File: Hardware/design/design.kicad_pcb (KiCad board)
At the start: 2 copper layers, 1 part

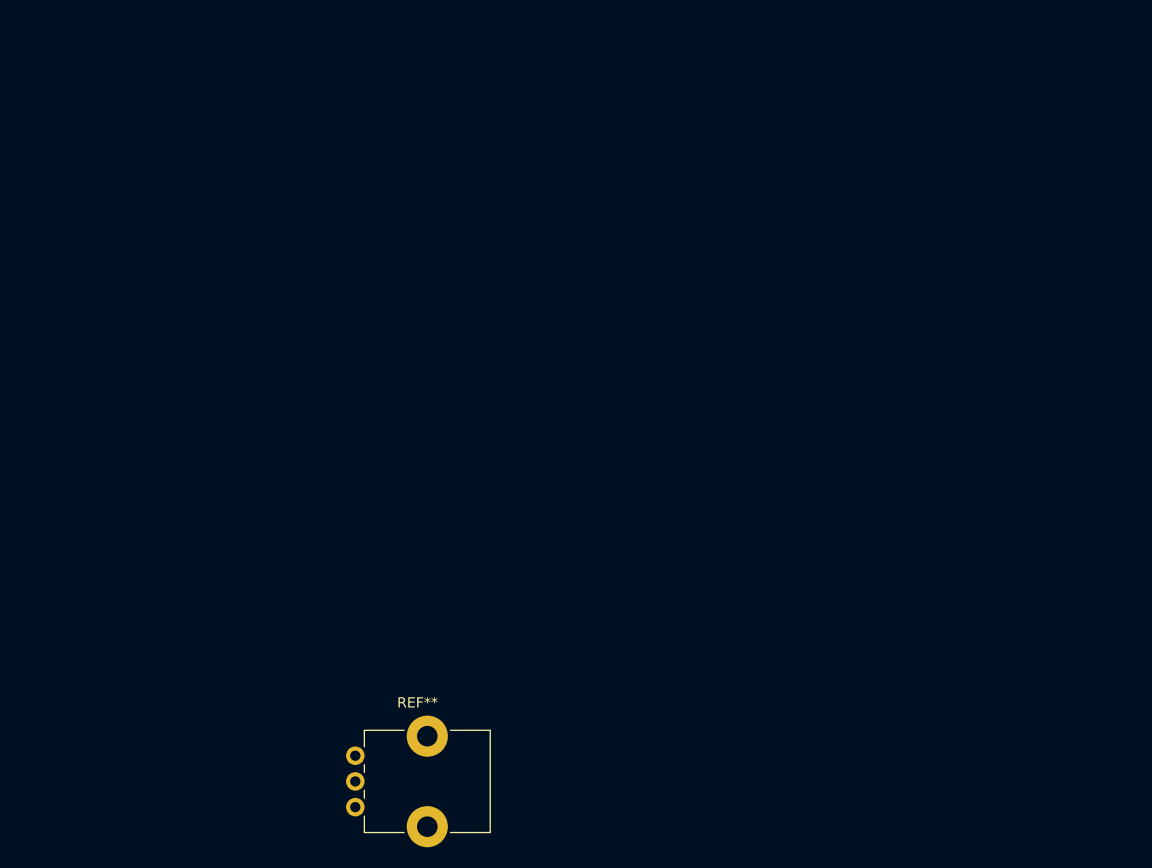
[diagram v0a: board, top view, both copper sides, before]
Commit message: chose and added 3 toggle switches
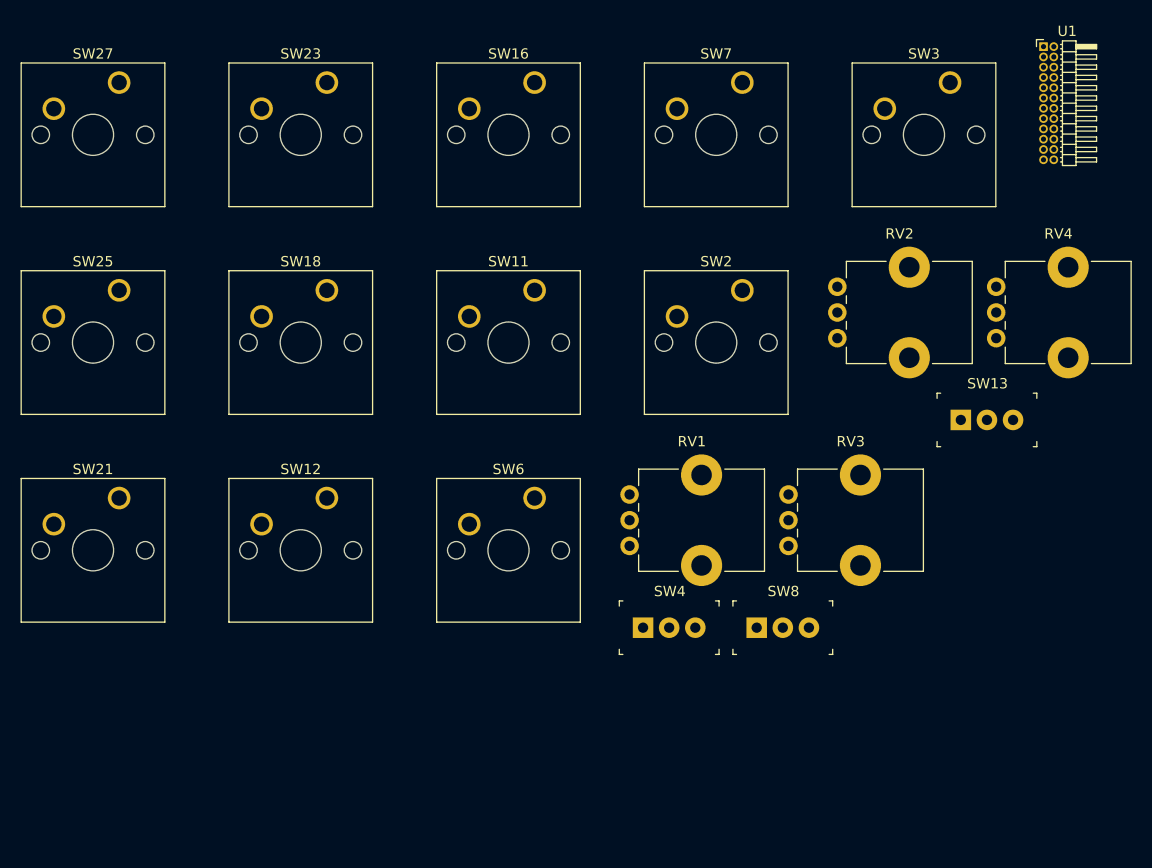
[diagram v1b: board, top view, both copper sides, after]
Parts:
- removed REF**: Potentiometer_Bourns_PTV09A-1_Single_Vertical, Potentiometer_THT:Potentiometer_Bourns_PTV09A-1_Single_Vertical
- added RV1: R_POT, Potentiometer_THT:Potentiometer_Bourns_PTV09A-1_Single_Vertical, F.Cu at (121.9, 52.1)
- added RV2: R_POT, Potentiometer_THT:Potentiometer_Bourns_PTV09A-1_Single_Vertical, F.Cu at (142.1, 31.9)
- added RV3: R_POT, Potentiometer_THT:Potentiometer_Bourns_PTV09A-1_Single_Vertical, F.Cu at (137.4, 52.1)
- added RV4: R_POT, Potentiometer_THT:Potentiometer_Bourns_PTV09A-1_Single_Vertical, F.Cu at (157.6, 31.9)
- added SW11: SW_Push, Button_Switch_Keyboard:SW_Cherry_MX_1.00u_PCB, F.Cu at (112.7, 27.2)
- added SW12: SW_Push, Button_Switch_Keyboard:SW_Cherry_MX_1.00u_PCB, F.Cu at (92.5, 47.4)
- added SW13: SW_Push, digikey-footprints:Switch_Toggle_ATE1D-2M3-10-Z, F.Cu at (156.7, 39.8)
- added SW16: SW_Push, Button_Switch_Keyboard:SW_Cherry_MX_1.00u_PCB, F.Cu at (112.7, 7.01)
- added SW18: SW_Push, Button_Switch_Keyboard:SW_Cherry_MX_1.00u_PCB, F.Cu at (92.5, 27.2)
- added SW2: SW_Push, Button_Switch_Keyboard:SW_Cherry_MX_1.00u_PCB, F.Cu at (132.9, 27.2)
- added SW21: SW_Push, Button_Switch_Keyboard:SW_Cherry_MX_1.00u_PCB, F.Cu at (72.3, 47.4)
- added SW23: SW_Push, Button_Switch_Keyboard:SW_Cherry_MX_1.00u_PCB, F.Cu at (92.5, 7.01)
- added SW25: SW_Push, Button_Switch_Keyboard:SW_Cherry_MX_1.00u_PCB, F.Cu at (72.3, 27.2)
- added SW27: SW_Push, Button_Switch_Keyboard:SW_Cherry_MX_1.00u_PCB, F.Cu at (72.3, 7.01)
- added SW3: SW_Push, Button_Switch_Keyboard:SW_Cherry_MX_1.00u_PCB, F.Cu at (153.1, 7.01)
- added SW4: SW_Push, digikey-footprints:Switch_Toggle_ATE1D-2M3-10-Z, F.Cu at (125.8, 60.0)
- added SW6: SW_Push, Button_Switch_Keyboard:SW_Cherry_MX_1.00u_PCB, F.Cu at (112.7, 47.4)
- added SW7: SW_Push, Button_Switch_Keyboard:SW_Cherry_MX_1.00u_PCB, F.Cu at (132.9, 7.01)
- added SW8: SW_Push, digikey-footprints:Switch_Toggle_ATE1D-2M3-10-Z, F.Cu at (136.8, 60.0)
- added U1: ProMicro, Connector_PinHeader_1.00mm:PinHeader_2x12_P1.00mm_Horizontal, F.Cu at (162.2, 3.52)

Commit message: chose rotary switches and diodes, organized layout a bit
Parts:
- added D1: DIODE, Diode_THT:D_5KPW_P7.62mm_Vertical_AnodeUp, F.Cu at (397.5, 88.9)
- added D10: DIODE, Diode_THT:D_5KPW_P7.62mm_Vertical_AnodeUp, F.Cu at (378.5, 74.9)
- added D11: DIODE, Diode_THT:D_5KPW_P7.62mm_Vertical_AnodeUp, F.Cu at (396.2, 58.4)
- added D12: DIODE, Diode_THT:D_5KPW_P7.62mm_Vertical_AnodeUp, F.Cu at (359.4, 74.9)
- added D13: DIODE, Diode_THT:D_5KPW_P7.62mm_Vertical_AnodeUp, F.Cu at (38.1, 157.5)
- added D14: DIODE, Diode_THT:D_5KPW_P7.62mm_Vertical_AnodeUp, F.Cu at (35.6, 193.0)
- added D15: DIODE, Diode_THT:D_5KPW_P7.62mm_Vertical_AnodeUp, F.Cu at (33.0, 229.9)
- added D16: DIODE, Diode_THT:D_5KPW_P7.62mm_Vertical_AnodeUp, F.Cu at (29.2, 265.4)
- added D17: DIODE, Diode_THT:D_5KPW_P7.62mm_Vertical_AnodeUp, F.Cu at (58.4, 157.5)
- added D18: DIODE, Diode_THT:D_5KPW_P7.62mm_Vertical_AnodeUp, F.Cu at (57.1, 194.3)
- added D19: DIODE, Diode_THT:D_5KPW_P7.62mm_Vertical_AnodeUp, F.Cu at (55.9, 229.9)
- added D2: DIODE, Diode_THT:D_5KPW_P7.62mm_Vertical_AnodeUp, F.Cu at (378.5, 105.4)
- added D20: DIODE, Diode_THT:D_5KPW_P7.62mm_Vertical_AnodeUp, F.Cu at (53.3, 265.4)
- added D21: DIODE, Diode_THT:D_5KPW_P7.62mm_Vertical_AnodeUp, F.Cu at (81.3, 157.5)
- added D22: DIODE, Diode_THT:D_5KPW_P7.62mm_Vertical_AnodeUp, F.Cu at (78.7, 194.3)
- added D23: DIODE, Diode_THT:D_5KPW_P7.62mm_Vertical_AnodeUp, F.Cu at (77.5, 227.3)
- added D24: DIODE, Diode_THT:D_5KPW_P7.62mm_Vertical_AnodeUp, F.Cu at (74.9, 265.4)
- added D25: DIODE, Diode_THT:D_5KPW_P7.62mm_Vertical_AnodeUp, F.Cu at (101.6, 160.0)
- added D26: DIODE, Diode_THT:D_5KPW_P7.62mm_Vertical_AnodeUp, F.Cu at (99.1, 194.3)
- added D27: DIODE, Diode_THT:D_5KPW_P7.62mm_Vertical_AnodeUp, F.Cu at (99.1, 228.6)
- added D28: DIODE, Diode_THT:D_5KPW_P7.62mm_Vertical_AnodeUp, F.Cu at (97.8, 264.2)
- added D29: DIODE, Diode_THT:D_5KPW_P7.62mm_Vertical_AnodeUp, F.Cu at (120.7, 160.0)
- added D3: DIODE, Diode_THT:D_5KPW_P7.62mm_Vertical_AnodeUp, F.Cu at (377.2, 88.9)
- added D30: DIODE, Diode_THT:D_5KPW_P7.62mm_Vertical_AnodeUp, F.Cu at (120.7, 194.3)
- added D31: DIODE, Diode_THT:D_5KPW_P7.62mm_Vertical_AnodeUp, F.Cu at (120.7, 228.6)
- added D32: DIODE, Diode_THT:D_5KPW_P7.62mm_Vertical_AnodeUp, F.Cu at (119.4, 264.2)
- added D33: DIODE, Diode_THT:D_5KPW_P7.62mm_Vertical_AnodeUp, F.Cu at (144.8, 160.0)
- added D34: DIODE, Diode_THT:D_5KPW_P7.62mm_Vertical_AnodeUp, F.Cu at (142.2, 194.3)
- added D35: DIODE, Diode_THT:D_5KPW_P7.62mm_Vertical_AnodeUp, F.Cu at (142.2, 228.6)
- added D36: DIODE, Diode_THT:D_5KPW_P7.62mm_Vertical_AnodeUp, F.Cu at (141.0, 265.4)
- added D4: DIODE, Diode_THT:D_5KPW_P7.62mm_Vertical_AnodeUp, F.Cu at (358.1, 105.4)
- added D5: DIODE, Diode_THT:D_5KPW_P7.62mm_Vertical_AnodeUp, F.Cu at (358.1, 88.9)
- added D6: DIODE, Diode_THT:D_5KPW_P7.62mm_Vertical_AnodeUp, F.Cu at (397.5, 105.4)
- added D7: DIODE, Diode_THT:D_5KPW_P7.62mm_Vertical_AnodeUp, F.Cu at (359.4, 58.4)
- added D8: DIODE, Diode_THT:D_5KPW_P7.62mm_Vertical_AnodeUp, F.Cu at (397.5, 74.9)
- added D9: DIODE, Diode_THT:D_5KPW_P7.62mm_Vertical_AnodeUp, F.Cu at (377.2, 58.4)
- added SW1: NKK_NR01, Kicad_Akiyuki_Footprint:NR01, F.Cu at (341.6, 90.2)
- added SW10: NKK_NR01, Kicad_Akiyuki_Footprint:NR01, F.Cu at (341.6, 105.4)
- added SW14: SW_Push, Button_Switch_Keyboard:SW_Cherry_MX_1.00u_PCB, F.Cu at (76.2, 280.7)
- added SW15: NKK_NR01, Kicad_Akiyuki_Footprint:NR01, F.Cu at (341.6, 59.7)
- added SW17: SW_Push, Button_Switch_Keyboard:SW_Cherry_MX_1.00u_PCB, F.Cu at (102.9, 242.6)
- added SW19: SW_Push, Button_Switch_Keyboard:SW_Cherry_MX_1.00u_PCB, F.Cu at (100.3, 278.1)
- added SW20: NKK_NR01, Kicad_Akiyuki_Footprint:NR01, F.Cu at (341.6, 74.9)
- added SW22: SW_Push, Button_Switch_Keyboard:SW_Cherry_MX_1.00u_PCB, F.Cu at (125.7, 242.6)
- added SW24: SW_Push, Button_Switch_Keyboard:SW_Cherry_MX_1.00u_PCB, F.Cu at (123.2, 278.1)
- added SW26: SW_Push, Button_Switch_Keyboard:SW_Cherry_MX_1.00u_PCB, F.Cu at (144.8, 242.6)
- added SW28: SW_Push, Button_Switch_Keyboard:SW_Cherry_MX_1.00u_PCB, F.Cu at (146.1, 278.1)
- added SW5: SW_Push, digikey-footprints:Tilt_Switch_RB-220-07A_R, F.Cu at (29.2, 283.2)
- added SW9: SW_Push, digikey-footprints:Tilt_Switch_RB-220-07A_R, F.Cu at (53.3, 281.9)
- U1: footprint Connector_PinHeader_1.00mm:PinHeader_2x12_P1.00mm_Horizontal -> promicro:ProMicro
- moved SW3 227.2 mm to (40.6, 204.5)
- moved SW13 218.4 mm to (78.7, 243.8)
- moved SW27 212.4 mm to (147.3, 205.7)
- moved SW7 209.7 mm to (62.2, 204.5)
- moved SW4 204.8 mm to (35.6, 243.8)
- moved SW23 201.5 mm to (125.7, 205.7)
- moved SW8 199.8 mm to (58.4, 243.8)
- moved SW18 178.9 mm to (104.1, 205.7)
- moved SW2 171.6 mm to (41.9, 172.7)
- moved SW16 165.8 mm to (106.7, 172.7)
- moved SW25 164.3 mm to (148.6, 172.7)
- moved RV4 162.9 mm to (232.4, 176.5)
- moved SW12 157.4 mm to (82.5, 204.5)
- moved RV2 154.7 mm to (232.4, 157.5)
- moved SW11 148.3 mm to (83.8, 172.7)
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
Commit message: semi-linearized switch matrix into 2 octave layout
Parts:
- SW13, SW4, SW8: footprint digikey-footprints:Switch_Toggle_ATE1D-2M3-10-Z -> Button_Switch_Keyboard:SW_Cherry_MX_1.00u_PCB
- SW5, SW9: footprint digikey-footprints:Tilt_Switch_RB-220-07A_R -> Button_Switch_Keyboard:SW_Cherry_MX_1.00u_PCB
- moved SW25 231.8 mm to (-83.0, 180.5)
- moved SW21 229.2 mm to (-102.1, 180.5)
- moved D33 228.7 mm to (-83.0, 180.5)
- moved D29 223.7 mm to (-102.1, 180.5)
- moved SW16 218.6 mm to (-111.6, 161.5)
- moved D25 213.2 mm to (-111.6, 161.5)
- moved SW11 205.1 mm to (-121.1, 180.5)
- moved D21 203.7 mm to (-121.1, 180.5)
- moved SW6 193.2 mm to (-130.7, 161.5)
- moved D17 189.1 mm to (-130.7, 161.5)
- moved SW2 182.3 mm to (-140.2, 180.5)
- moved D13 179.8 mm to (-140.2, 180.5)
- moved SW27 175.0 mm to (-25.9, 180.5)
- moved D34 168.7 mm to (-25.9, 180.5)
- moved SW23 167.1 mm to (-35.4, 161.5)
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
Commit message: columns routed together
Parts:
- moved D32 5.68 mm to (95.4, 166.6)
- moved D28 1.56 mm to (88.4, 180.5)
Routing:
- net /ROW1: track 0.00 -> 115.0 mm
- net /ROW3: track 0.00 -> 115.0 mm
- net /ROW2: track 0.00 -> 112.6 mm
- net /ROW0: track 0.00 -> 111.2 mm

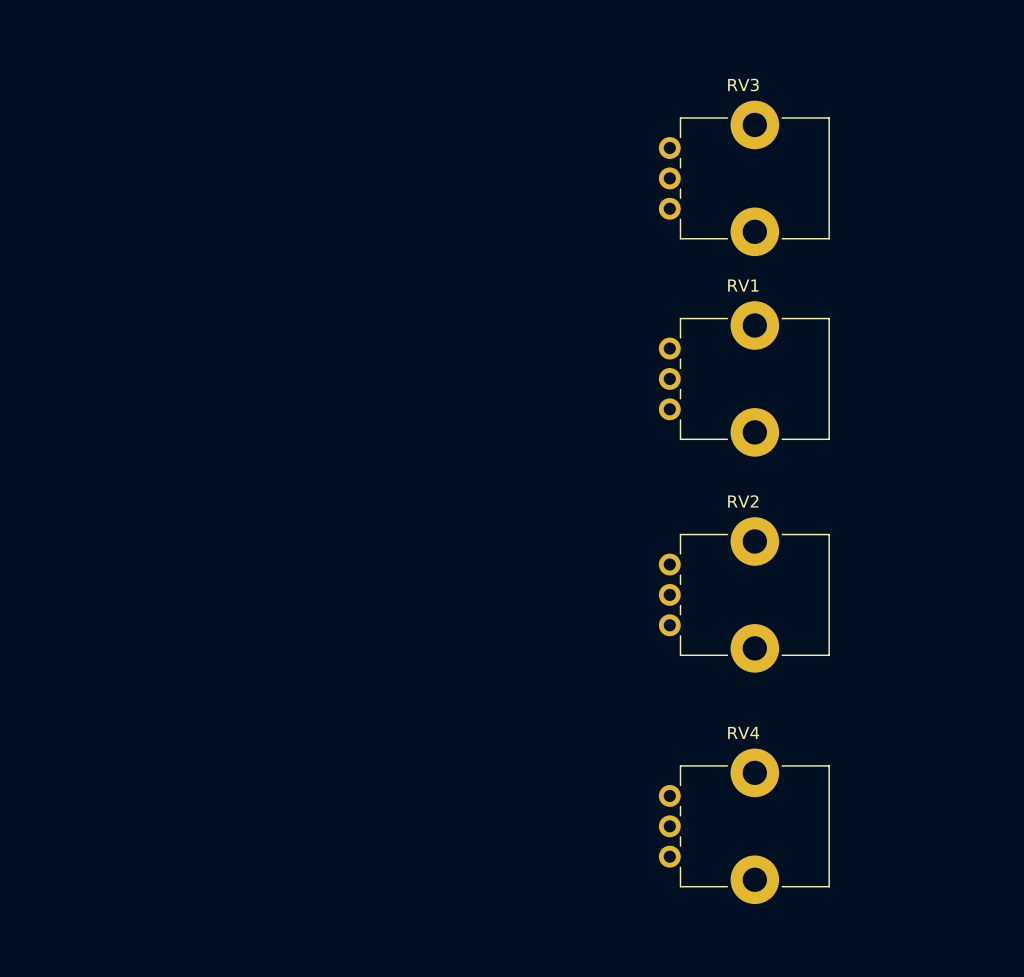
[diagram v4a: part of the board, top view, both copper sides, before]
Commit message: routed vcc and gnd for pots
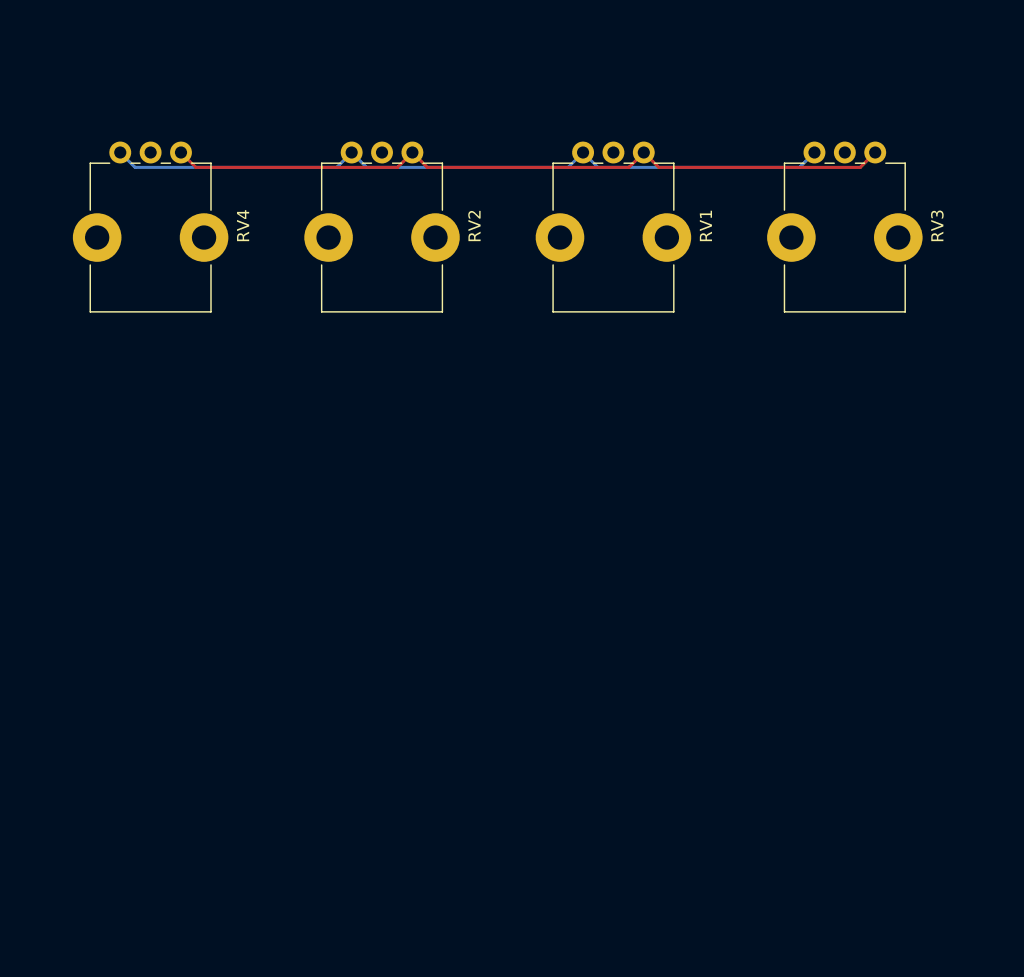
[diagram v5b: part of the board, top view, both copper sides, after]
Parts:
- moved RV4 73.5 mm to (187.2, 118.6), turned to 270 degrees
- moved RV2 46.9 mm to (206.2, 118.6), turned to 270 degrees
- moved RV1 22.3 mm to (225.3, 118.6), turned to 270 degrees
- moved RV3 12.8 mm to (244.3, 118.6), turned to 270 degrees
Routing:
- net /VCC: track 0.00 -> 60.2 mm
- net /GND: track 0.00 -> 60.2 mm

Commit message: a less elegant solution to column routing
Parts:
- moved D32 5.68 mm to (97.9, 161.5)
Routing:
- net /COL3: track 0.00 -> 265.3 mm, vias 0 -> 7
- net /COL1: track 0.00 -> 247.3 mm, vias 0 -> 7
- net /COL0: track 0.00 -> 245.6 mm, vias 0 -> 3
- net /COL4: track 0.00 -> 237.8 mm, vias 0 -> 3
- net /COL2: track 0.00 -> 237.6 mm, vias 0 -> 7
- net /COL5: track 0.00 -> 229.8 mm, vias 0 -> 3
- net /GND: track 60.2 -> 79.0 mm
- net /ROW2: track 112.6 -> 111.0 mm

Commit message: finished column routing, sitched to 1206 SMD diodes
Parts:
- D1, D10, D11, D12, D13, D14, D15, D16, D17, D18, D19, D2, D20, D21, D22, D23, D24, D25, D26, D27, D28, D29, D3, D30, D31, D32, D33, D34, D35, D36, D4, D5, D6, D7, D8, D9: footprint Diode_THT:D_5KPW_P7.62mm_Vertical_AnodeUp -> Diode_SMD:D_1206_3216Metric
- moved D13 202.0 mm to (21.4, 59.3), turned to 270 degrees
- moved D14 202.0 mm to (88.0, 40.2), turned to 270 degrees
- moved D15 202.0 mm to (154.7, 59.3), turned to 270 degrees
- moved D16 202.0 mm to (221.4, 40.2), turned to 270 degrees
- moved D17 202.0 mm to (30.9, 40.2), turned to 270 degrees
- moved D18 202.0 mm to (97.6, 59.3), turned to 270 degrees
- moved D19 202.0 mm to (164.2, 40.2), turned to 270 degrees
- moved D20 202.0 mm to (230.9, 59.3), turned to 270 degrees
- moved D21 202.0 mm to (40.4, 59.3), turned to 270 degrees
- moved D22 202.0 mm to (107.1, 40.2), turned to 270 degrees
- moved D23 202.0 mm to (173.8, 59.3), turned to 270 degrees
- moved D24 202.0 mm to (240.4, 40.2), turned to 270 degrees
- moved D25 202.0 mm to (49.9, 40.2), turned to 270 degrees
- moved D26 202.0 mm to (116.6, 59.3), turned to 270 degrees
- moved D27 202.0 mm to (183.3, 40.2), turned to 270 degrees
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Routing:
- net /COL5: track 229.8 -> 218.2 mm, vias 3 -> 4
- net Net-(D23-Pad1): track 0.00 -> 7.58 mm
- net Net-(D16-Pad1): track 0.00 -> 7.58 mm
- net Net-(D26-Pad1): track 0.00 -> 7.58 mm
- net Net-(D14-Pad1): track 0.00 -> 7.58 mm
- net Net-(D13-Pad1): track 0.00 -> 7.58 mm
- net Net-(D29-Pad1): track 0.00 -> 7.58 mm
- net Net-(D25-Pad1): track 0.00 -> 7.58 mm
- net Net-(D21-Pad1): track 0.00 -> 7.58 mm
- net Net-(D17-Pad1): track 0.00 -> 7.58 mm
- net Net-(D35-Pad1): track 0.00 -> 7.58 mm
- net Net-(D34-Pad1): track 0.00 -> 7.58 mm
- net Net-(D33-Pad1): track 0.00 -> 7.58 mm
- net Net-(D32-Pad1): track 0.00 -> 7.58 mm
- net Net-(D31-Pad1): track 0.00 -> 7.58 mm
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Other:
- board outline added: 304.8 x 76.2 mm

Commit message: routed all cherry switches and pots, fixed issue with rotary switch nets in schematic
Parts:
- moved D1 141.3 mm to (282.0, 9.96)
- moved D10 141.3 mm to (251.8, 1.43)
- moved D11 141.3 mm to (266.1, -21.1)
- moved D2 141.3 mm to (238.8, 27.7)
- moved D3 141.3 mm to (259.1, 11.2)
- moved D4 141.3 mm to (259.1, 27.7)
- moved D6 141.3 mm to (279.5, 27.7)
- moved D7 141.3 mm to (238.3, -21.0)
- moved D9 141.3 mm to (252.1, -21.1)
- moved D12 141.3 mm to (239.0, 0.80)
- moved D5 141.3 mm to (238.3, 10.4)
- moved D8 141.3 mm to (265.9, 1.18)
- moved SW1 141.3 mm to (223.6, 12.5)
- moved SW10 141.3 mm to (223.6, 27.7)
- moved SW15 141.3 mm to (223.6, -18.0)
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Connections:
- D1 pad 2: /col0 -> /COL0
- D10 pad 2: /col4 -> /COL4
- D11 pad 2: /col5 -> /COL5
- D12 pad 2: /col3 -> /COL3
- D2 pad 2: /col0 -> /COL0
- D3 pad 2: /col1 -> /COL1
- D4 pad 2: /col1 -> /COL1
- D5 pad 2: /col2 -> /COL2
- D6 pad 2: /col2 -> /COL2
- D7 pad 2: /col3 -> /COL3
- D8 pad 2: /col5 -> /COL5
- D9 pad 2: /col4 -> /COL4
- SW1 pad 3: /row5 -> /ROW5
- SW1 pad 5: Net-(SW1-Pad5) -> (no net)
- SW1 pad 6: Net-(SW1-Pad6) -> (no net)
- SW10 pad 3: /row4 -> /ROW4
- SW10 pad 5: Net-(SW10-Pad5) -> (no net)
- SW10 pad 6: Net-(SW10-Pad6) -> (no net)
- SW15 pad 3: /row5 -> /ROW5
- SW15 pad 5: Net-(SW15-Pad5) -> (no net)
- SW15 pad 6: Net-(SW15-Pad6) -> (no net)
- SW20 pad 3: /row4 -> /ROW4
- SW20 pad 5: Net-(SW20-Pad5) -> (no net)
- SW20 pad 6: Net-(SW20-Pad6) -> (no net)
- U1 pad 1: Net-(U1-Pad1) -> (no net)
- U1 pad 2: Net-(U1-Pad2) -> (no net)
- U1 pad 22: /RST -> (no net)
- U1 pad 24: /RAW -> (no net)
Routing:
- net /ROW3: track 115.0 -> 325.5 mm, vias 0 -> 2
- net /ROW2: track 111.0 -> 263.0 mm, vias 0 -> 2
- net /A3: track 0.00 -> 115.5 mm
- net /A2: track 0.00 -> 93.5 mm
- net /COL5: track 218.2 -> 304.9 mm, vias 4 -> 5
- net /A1: track 0.00 -> 71.9 mm
- net /COL0: track 245.3 -> 315.0 mm
- net /ROW1: track 115.0 -> 184.3 mm
- net /COL2: track 241.7 -> 310.0 mm, vias 10 -> 11
- net /COL4: track 244.3 -> 310.7 mm, vias 5 -> 6
- net /COL3: track 270.7 -> 325.4 mm
- net /GND: track 79.0 -> 131.5 mm
- net /VCC: track 60.2 -> 112.0 mm
- net /A0: track 0.00 -> 50.5 mm
- net /COL1: track 251.5 -> 292.3 mm
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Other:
- board size 304.8 x 76.2 mm -> 285.8 x 76.2 mm
